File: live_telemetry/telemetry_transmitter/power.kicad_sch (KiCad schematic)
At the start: 14 parts, among them U3 SPX3819M5-L-3-3/TR, U5 INA180, U6 AP1509-50SG-13

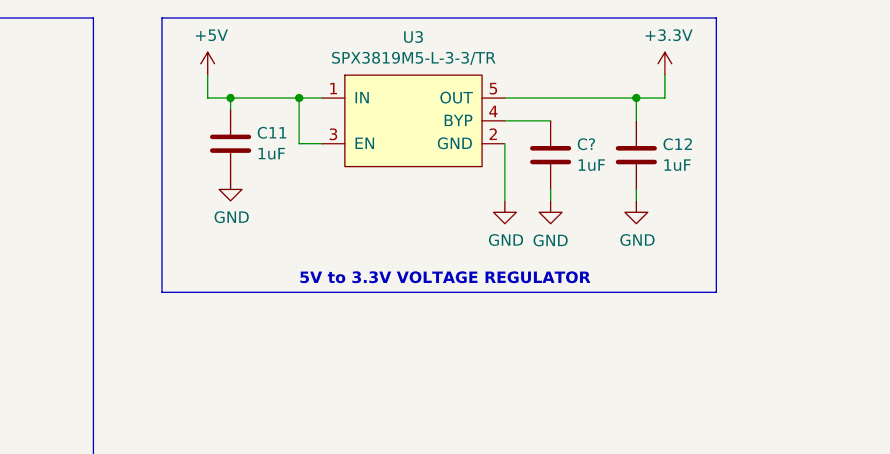
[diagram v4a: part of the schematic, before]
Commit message: Updated cap values
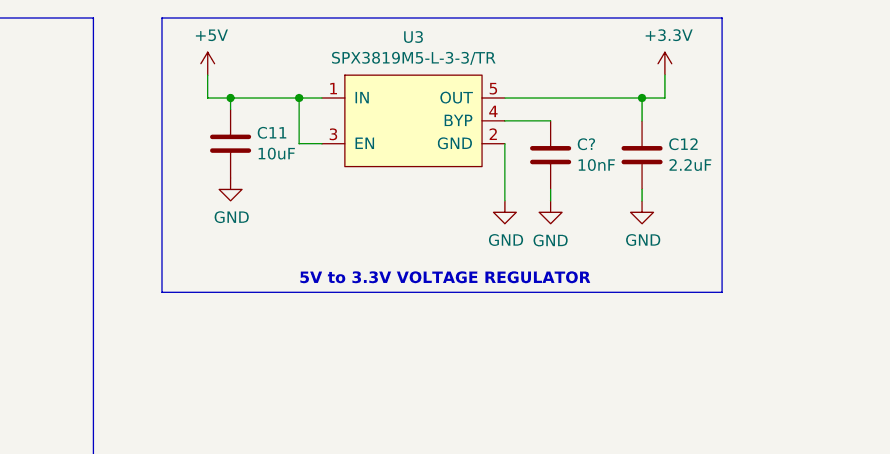
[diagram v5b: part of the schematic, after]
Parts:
- C11: value 1uF -> 10uF
- C12: value 1uF -> 2.2uF
- C?: value 1uF -> 10nF
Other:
- moved on the sheet: C12
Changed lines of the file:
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@@
     (rev "2.1")
   )
-  (junction (at 228.6 71.12) (diameter 0) (color 0 0 0 0)
-  )
   (junction (at 111.76 92.71) (diameter 0) (color 0 0 0 0)
   )
   (junction (at 90.17 127) (diameter 0) (color 0 0 0 0)
   )
+  (junction (at 229.235 71.12) (diameter 0) (color 0 0 0 0)
+  )
   (junction (at 191.135 71.12) (diameter 0) (color 0 0 0 0)
   )
@@
     (stroke (width 0) (type default) (color 0 0 0 0))
   )
-  (polyline (pts (xy 175.895 92.71) (xy 237.49 92.71))
+  (polyline (pts (xy 175.895 92.71) (xy 238.125 92.71))
     (stroke (width 0) (type default) (color 0 0 0 0))
   )
@@
     (stroke (width 0) (type default) (color 0 0 0 0))
   )
+  (wire (pts (xy 229.235 71.12) (xy 229.235 73.66))
+    (stroke (width 0) (type default) (color 0 0 0 0))
+  )
   (wire (pts (xy 193.675 76.2) (xy 191.135 76.2))
     (stroke (width 0) (type default) (color 0 0 0 0))
@@
     (stroke (width 0) (type default) (color 0 0 0 0))
   )
-  (polyline (pts (xy 237.49 62.23) (xy 175.895 62.23))
+  (polyline (pts (xy 238.125 62.23) (xy 175.895 62.23))
     (stroke (width 0) (type default) (color 0 0 0 0))
   )
@@
     (stroke (width 0) (type default) (color 0 0 0 0))
   )
-  (wire (pts (xy 228.6 71.12) (xy 228.6 73.66))
-    (stroke (width 0) (type default) (color 0 0 0 0))
-  )
   (wire (pts (xy 63.5 90.17) (xy 63.5 95.25))
     (stroke (width 0) (type default) (color 0 0 0 0))
@@
     (stroke (width 0) (type default) (color 0 0 0 0))
   )
-  (wire (pts (xy 228.6 81.28) (xy 228.6 82.55))
+  (wire (pts (xy 229.235 81.28) (xy 229.235 82.55))
     (stroke (width 0) (type default) (color 0 0 0 0))
   )
@@
     (stroke (width 0) (type default) (color 0 0 0 0))
   )
-  (wire (pts (xy 213.995 71.12) (xy 228.6 71.12))
-    (stroke (width 0) (type default) (color 0 0 0 0))
-  )
   (wire (pts (xy 180.975 71.12) (xy 183.515 71.12))
     (stroke (width 0) (type default) (color 0 0 0 0))
@@
     (stroke (width 0) (type default) (color 0 0 0 0))
   )
-  (polyline (pts (xy 237.49 92.71) (xy 237.49 62.23))
+  (polyline (pts (xy 238.125 92.71) (xy 238.125 62.23))
     (stroke (width 0) (type default) (color 0 0 0 0))
   )
@@
     (stroke (width 0) (type default) (color 0 0 0 0))
   )
+  (wire (pts (xy 229.235 71.12) (xy 231.775 71.12))
+    (stroke (width 0) (type default) (color 0 0 0 0))
+  )
   (wire (pts (xy 77.47 72.39) (xy 77.47 82.55))
     (stroke (width 0) (type default) (color 0 0 0 0))
@@
     (stroke (width 0) (type default) (color 0 0 0 0))
   )
-  (wire (pts (xy 228.6 71.12) (xy 231.775 71.12))
+  (wire (pts (xy 213.995 71.12) (xy 229.235 71.12))
     (stroke (width 0) (type default) (color 0 0 0 0))
   )
@@
       (effects (font (size 1.27 1.27)) (justify right))
     )
-    (property "Value" "1uF" (id 1) (at 186.436 77.343 0)
+    (property "Value" "10uF" (id 1) (at 186.436 77.343 0)
       (effects (font (size 1.27 1.27)) (justify right))
     )
@@
     (pin "2")
   )
-  (symbol (lib_id "Device:C") (at 228.6 77.47 180) (unit 1)
-    (in_bom yes) (on_board yes)
-    (property "Reference" "C12" (id 0) (at 231.521 76.3016 0)
-      (effects (font (size 1.27 1.27)) (justify right))
-    )
-    (property "Value" "1uF" (id 1) (at 231.521 78.613 0)
-      (effects (font (size 1.27 1.27)) (justify right))
-    )
-    (property "Footprint" "Capacitor_SMD:C_0805_2012Metric_Pad1.15x1.40mm_HandSolder" (id 2) (at 227.6348 73.66 0)
-      (effects (font (size 1.27 1.27)) hide)
-    )
-    (property "Datasheet" "~" (id 3) (at 228.6 77.47 0)
+  (symbol (lib_id "Device:C") (at 229.235 77.47 180) (unit 1)
+    (in_bom yes) (on_board yes)
+    (property "Reference" "C12" (id 0) (at 232.156 76.3016 0)
+      (effects (font (size 1.27 1.27)) (justify right))
+    )
+    (property "Value" "2.2uF" (id 1) (at 232.156 78.613 0)
+      (effects (font (size 1.27 1.27)) (justify right))
+    )
+    (property "Footprint" "Capacitor_SMD:C_0805_2012Metric_Pad1.15x1.40mm_HandSolder" (id 2) (at 228.2698 73.66 0)
+      (effects (font (size 1.27 1.27)) hide)
+    )
+    (property "Datasheet" "~" (id 3) (at 229.235 77.47 0)
       (effects (font (size 1.27 1.27)) hide)
     )
@@
     (pin "1")
   )
-  (symbol (lib_id "power:GND") (at 228.6 82.55 0) (unit 1)
-    (in_bom yes) (on_board yes)
-    (property "Reference" "#PWR045" (id 0) (at 228.6 88.9 0)
-      (effects (font (size 1.27 1.27)) hide)
-    )
-    (property "Value" "GND" (id 1) (at 228.727 86.9442 0))
-    (property "Footprint" "" (id 2) (at 228.6 82.55 0)
-      (effects (font (size 1.27 1.27)) hide)
-    )
-    (property "Datasheet" "" (id 3) (at 228.6 82.55 0)
+  (symbol (lib_id "power:GND") (at 229.235 82.55 0) (unit 1)
+    (in_bom yes) (on_board yes)
+    (property "Reference" "#PWR045" (id 0) (at 229.235 88.9 0)
+      (effects (font (size 1.27 1.27)) hide)
+    )
+    (property "Value" "GND" (id 1) (at 229.362 86.9442 0))
+    (property "Footprint" "" (id 2) (at 229.235 82.55 0)
+      (effects (font (size 1.27 1.27)) hide)
+    )
+    (property "Datasheet" "" (id 3) (at 229.235 82.55 0)
       (effects (font (size 1.27 1.27)) hide)
     )
@@
       (effects (font (size 1.27 1.27)) (justify right))
     )
-    (property "Value" "1uF" (id 1) (at 221.996 78.613 0)
-      (effects (font (size 1.27 1.27)) (justify right))
-    )
+    (property "Value" "10nF" (id 1) (at 221.996 78.613 0)
+      (effects (font (size 1.27 1.27)) (justify right))
+    )

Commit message: new ltt layout
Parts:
- U3: footprint Package_TO_SOT_SMD:SOT-23-5_HandSoldering -> Package_TO_SOT_SMD:SOT-23-5; symbol canhw:TLV70233QDBVRQ1 -> Regulator_Linear:SPX3819M5-L-3-3
- gave numbers to parts that had none: 1
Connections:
- net +3.3V is gone; now on net +3V3: C7.2, U5.5 (VS)
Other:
- moved on the sheet: U3
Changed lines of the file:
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@@
   (junction (at 95.25 127) (diameter 0) (color 0 0 0 0)
   )
-  (wire (pts (xy 213.995 73.66) (xy 219.075 73.66))
+  (wire (pts (xy 211.455 73.66) (xy 219.075 73.66))
     (stroke (width 0) (type default) (color 0 0 0 0))
   )
@@
     (stroke (width 0) (type default) (color 0 0 0 0))
   )
-  (wire (pts (xy 193.675 76.2) (xy 191.135 76.2))
-    (stroke (width 0) (type default) (color 0 0 0 0))
-  )
   (wire (pts (xy 142.875 104.775) (xy 145.415 104.775))
     (stroke (width 0) (type default) (color 0 0 0 0))
@@
     (stroke (width 0) (type default) (color 0 0 0 0))
   )
-  (wire (pts (xy 213.995 76.2) (xy 213.995 82.55))
-    (stroke (width 0) (type default) (color 0 0 0 0))
-  )
   (wire (pts (xy 76.2 92.71) (xy 76.2 114.3))
     (stroke (width 0) (type default) (color 0 0 0 0))
@@
     (stroke (width 0) (type default) (color 0 0 0 0))
   )
+  (wire (pts (xy 203.835 82.55) (xy 203.835 81.28))
+    (stroke (width 0) (type default) (color 0 0 0 0))
+  )
   (wire (pts (xy 95.25 114.3) (xy 106.68 114.3))
     (stroke (width 0) (type default) (color 0 0 0 0))
@@
     (stroke (width 0) (type default) (color 0 0 0 0))
   )
-  (wire (pts (xy 231.775 68.58) (xy 231.775 71.12))
+  (wire (pts (xy 229.235 68.58) (xy 229.235 71.12))
     (stroke (width 0) (type default) (color 0 0 0 0))
   )
@@
     (stroke (width 0) (type default) (color 0 0 0 0))
   )
-  (wire (pts (xy 191.135 71.12) (xy 193.675 71.12))
-    (stroke (width 0) (type default) (color 0 0 0 0))
-  )
-  (wire (pts (xy 191.135 76.2) (xy 191.135 71.12))
-    (stroke (width 0) (type default) (color 0 0 0 0))
-  )
-  (wire (pts (xy 229.235 71.12) (xy 231.775 71.12))
+  (wire (pts (xy 191.135 71.12) (xy 196.215 71.12))
+    (stroke (width 0) (type default) (color 0 0 0 0))
+  )
+  (wire (pts (xy 191.135 73.66) (xy 191.135 71.12))
     (stroke (width 0) (type default) (color 0 0 0 0))
   )
@@
     (stroke (width 0) (type default) (color 0 0 0 0))
   )
+  (wire (pts (xy 196.215 73.66) (xy 191.135 73.66))
+    (stroke (width 0) (type default) (color 0 0 0 0))
+  )
   (wire (pts (xy 77.47 69.85) (xy 77.47 72.39))
     (stroke (width 0) (type default) (color 0 0 0 0))
@@
     (stroke (width 0) (type default) (color 0 0 0 0))
   )
-  (wire (pts (xy 213.995 71.12) (xy 229.235 71.12))
+  (wire (pts (xy 211.455 71.12) (xy 229.235 71.12))
     (stroke (width 0) (type default) (color 0 0 0 0))
   )
@@
     (pin "1")
   )
-  (symbol (lib_id "power:GND") (at 213.995 82.55 0) (unit 1)
-    (in_bom yes) (on_board yes)
-    (property "Reference" "#PWR044" (id 0) (at 213.995 88.9 0)
-      (effects (font (size 1.27 1.27)) hide)
-    )
-    (property "Value" "GND" (id 1) (at 214.122 86.9442 0))
-    (property "Footprint" "" (id 2) (at 213.995 82.55 0)
-      (effects (font (size 1.27 1.27)) hide)
-    )
-    (property "Datasheet" "" (id 3) (at 213.995 82.55 0)
+  (symbol (lib_id "power:GND") (at 203.835 82.55 0) (unit 1)
+    (in_bom yes) (on_board yes)
+    (property "Reference" "#PWR044" (id 0) (at 203.835 88.9 0)
+      (effects (font (size 1.27 1.27)) hide)
+    )
+    (property "Value" "GND" (id 1) (at 203.962 86.9442 0))
+    (property "Footprint" "" (id 2) (at 203.835 82.55 0)
+      (effects (font (size 1.27 1.27)) hide)
+    )
+    (property "Datasheet" "" (id 3) (at 203.835 82.55 0)
       (effects (font (size 1.27 1.27)) hide)
     )
@@
     )
     (property "Datasheet" "" (id 3) (at 183.515 80.01 0)
-      (effects (font (size 1.27 1.27)) hide)
-    )
-    (pin "1")
-  )
-  (symbol (lib_id "telemetry_transmitter-rescue:+3.3V-power") (at 231.775 68.58 0) (unit 1)
-    (in_bom yes) (on_board yes)
-    (property "Reference" "#PWR046" (id 0) (at 231.775 72.39 0)
-      (effects (font (size 1.27 1.27)) hide)
-    )
-    (property "Value" "+3.3V" (id 1) (at 232.156 64.1858 0))
-    (property "Footprint" "" (id 2) (at 231.775 68.58 0)
-      (effects (font (size 1.27 1.27)) hide)
-    )
-    (property "Datasheet" "" (id 3) (at 231.775 68.58 0)
       (effects (font (size 1.27 1.27)) hide)
     )
@@
     (pin "2")
   )
-  (symbol (lib_id "canhw:TLV70233QDBVRQ1") (at 203.835 80.01 0) (unit 1)
-    (in_bom yes) (on_board yes)
-    (property "Reference" "U3" (id 0) (at 203.835 64.389 0))
-    (property "Value" "SPX3819M5-L-3-3/TR" (id 1) (at 203.835 66.7004 0))
-    (property "Footprint" "Package_TO_SOT_SMD:SOT-23-5_HandSoldering" (id 2) (at 203.835 81.28 0)
-      (effects (font (size 1.27 1.27)) hide)
-    )
-    (property "Datasheet" "" (id 3) (at 203.835 81.28 0)
+  (symbol (lib_id "Regulator_Linear:SPX3819M5-L-3-3") (at 203.835 73.66 0) (unit 1)
+    (in_bom yes) (on_board yes)
+    (property "Reference" "U3" (id 0) (at 203.835 64.3636 0))
+    (property "Value" "SPX3819M5-L-3-3/TR" (id 1) (at 203.835 66.675 0))
+    (property "Footprint" "Package_TO_SOT_SMD:SOT-23-5" (id 2) (at 203.835 65.405 0)
+      (effects (font (size 1.27 1.27)) hide)
+    )
+    (property "Datasheet" "https://www.exar.com/content/document.ashx?id=22106&languageid=1033&type=Datasheet&partnumber=SPX3819&filename=SPX3819.pdf&part=SPX3819" (id 3) (at 203.835 73.66 0)
       (effects (font (size 1.27 1.27)) hide)
     )
@@
   (symbol (lib_id "Device:C") (at 219.075 77.47 180) (unit 1)
     (in_bom yes) (on_board yes)
-    (property "Reference" "C?" (id 0) (at 221.996 76.3016 0)
+    (property "Reference" "C8" (id 0) (at 221.996 76.3016 0)
       (effects (font (size 1.27 1.27)) (justify right))
     )
@@
   (symbol (lib_id "power:GND") (at 219.075 82.55 0) (unit 1)
     (in_bom yes) (on_board yes)
-    (property "Reference" "#PWR?" (id 0) (at 219.075 88.9 0)
+    (property "Reference" "#PWR028" (id 0) (at 219.075 88.9 0)
       (effects (font (size 1.27 1.27)) hide)
     )
@@
     (pin "1")
   )
-  (symbol (lib_id "power:+3.3V") (at 142.875 102.235 0) (unit 1)
+  (symbol (lib_id "power:+3V3") (at 142.875 102.235 0) (unit 1)
     (in_bom yes) (on_board yes) (fields_autoplaced)
-    (property "Reference" "#PWR?" (id 0) (at 142.875 106.045 0)
-      (effects (font (size 1.27 1.27)) hide)
-    )
-    (property "Value" "+3.3V" (id 1) (at 142.875 96.52 0))
+    (property "Reference" "#PWR0106" (id 0) (at 142.875 106.045 0)
+      (effects (font (size 1.27 1.27)) hide)
+    )
+    (property "Value" "+3V3" (id 1) (at 142.875 98.6592 0))
     (property "Footprint" "" (id 2) (at 142.875 102.235 0)
       (effects (font (size 1.27 1.27)) hide)
@@
       (effects (font (size 1.27 1.27)) hide)
     )
+    (pin "1")
+  )
+  (symbol (lib_id "power:+3V3") (at 229.235 68.58 0) (unit 1)
+    (in_bom yes) (on_board yes) (fields_autoplaced)
+    (property "Reference" "#PWR0105" (id 0) (at 229.235 72.39 0)
+      (effects (font (size 1.27 1.27)) hide)
+    )
+    (property "Value" "+3V3" (id 1) (at 229.235 65.0042 0))
+    (property "Footprint" "" (id 2) (at 229.235 68.58 0)
+      (effects (font (size 1.27 1.27)) hide)
+    )
+    (property "Datasheet" "" (id 3) (at 229.235 68.58 0)
+      (effects (font (size 1.27 1.27)) hide)
+    )

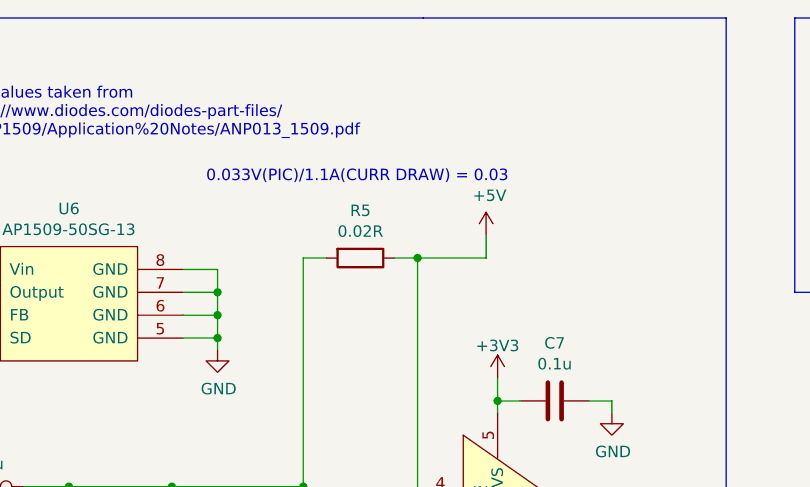
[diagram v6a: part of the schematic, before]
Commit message: update rsense based on stocked resistor
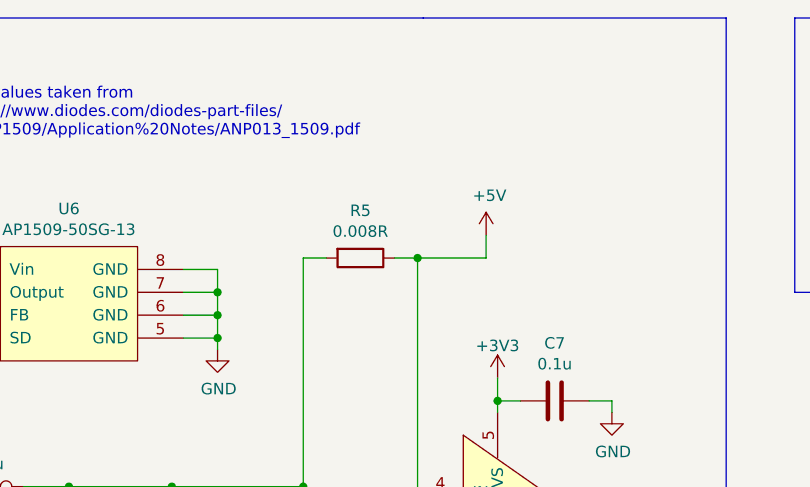
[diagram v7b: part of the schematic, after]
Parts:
- R5: value 0.02R -> 0.008R
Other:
- note removed: "0.033V(PIC)/1.1A(CURR DRAW) = 0.03"
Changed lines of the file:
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@@
     (effects (font (size 1.27 1.27) (thickness 0.254) bold) (justify left bottom))
-  )
-  (text "0.033V(PIC)/1.1A(CURR DRAW) = 0.03 " (at 110.49 80.645 0)
-    (effects (font (size 1.27 1.27)) (justify left bottom))
   )
   (hierarchical_label "CURR_LTT" (shape input) (at 156.845 117.475 0)
@@
     (in_bom yes) (on_board yes)
     (property "Reference" "R5" (id 0) (at 127.635 83.6422 90))
-    (property "Value" "0.02R" (id 1) (at 127.635 85.9536 90))
+    (property "Value" "0.008R" (id 1) (at 127.635 85.9536 90))
     (property "Footprint" "Resistor_SMD:R_1206_3216Metric_Pad1.42x1.75mm_HandSolder" (id 2) (at 127.635 87.122 90)
       (effects (font (size 1.27 1.27)) hide)
